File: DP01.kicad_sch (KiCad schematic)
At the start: 18 parts

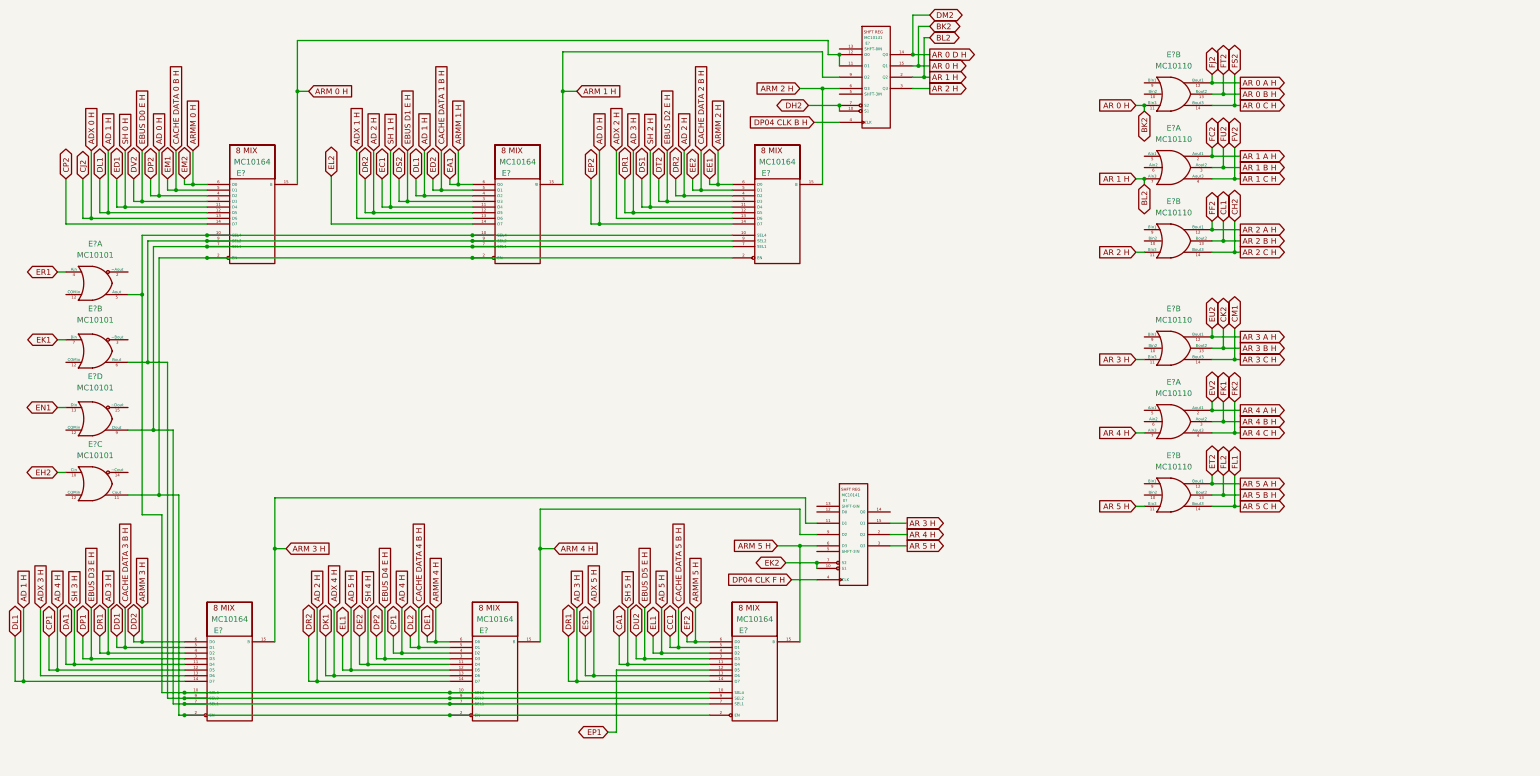
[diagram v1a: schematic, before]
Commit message: EDP is "done" but there is still much work to do to standardize and set up netlist export and verilog creation
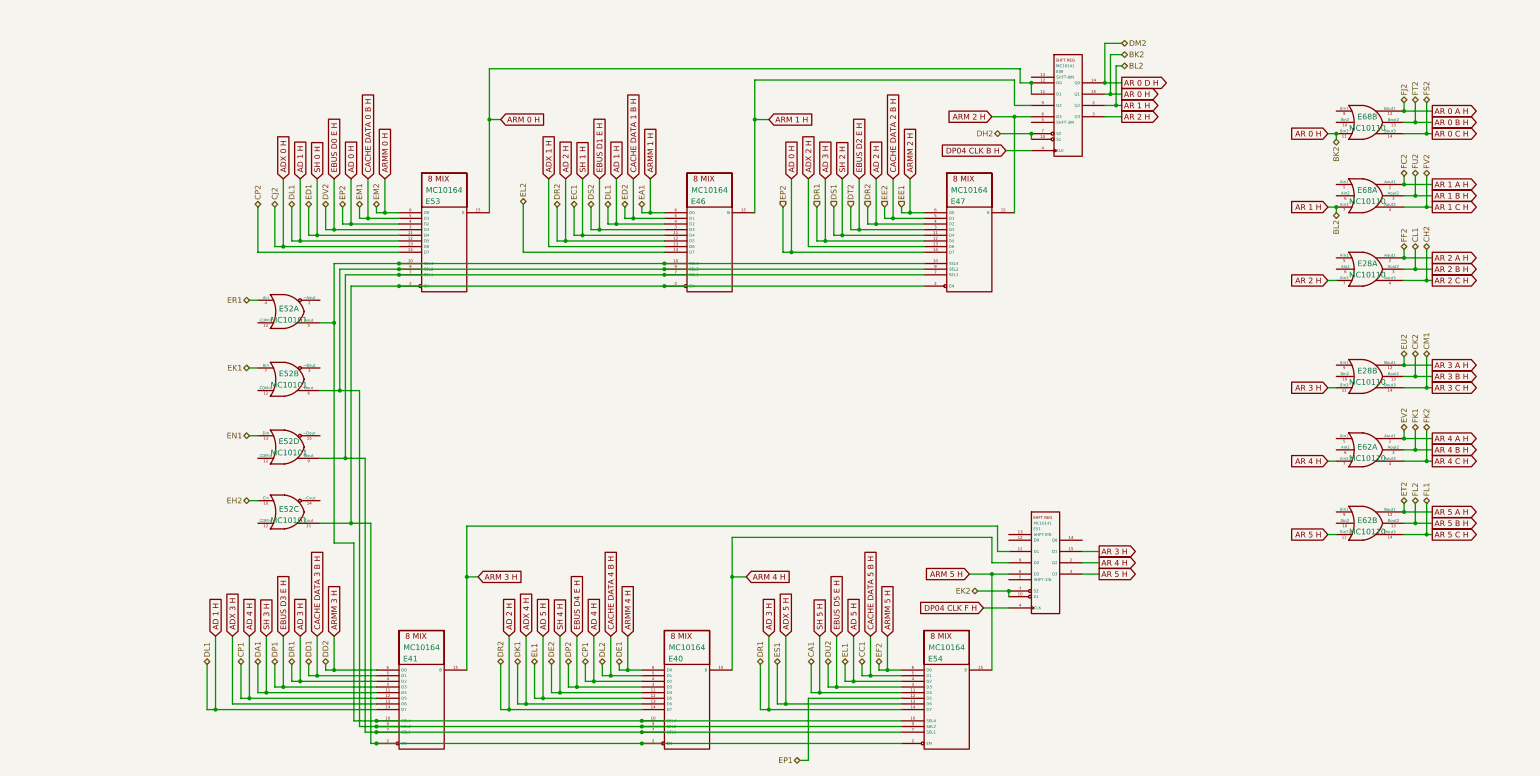
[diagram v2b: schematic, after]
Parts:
- gave numbers to parts that had none: 12
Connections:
- net AD 0 H: no longer E40.3 (D3)
- net AR 2 A H: now also E28.2 (Aout1); no longer E28.12 (Bout1)
- net AR 2 B H: now also E28.3 (Aout2); no longer E28.13 (Bout2)
- net AR 2 C H: now also E28.4 (Aout3); no longer E28.14 (Bout3)
- net AR 2 H: now also E28.7 (Ain3); no longer E28.11 (Bin3)
- net CA1 renamed SH 5 H
- net DA1 renamed SH 3 H
- net DE2 renamed SH 4 H
- net DP1 renamed EBUS D3 E H
- net DS1 renamed SH 2 H
- net DS2 renamed EBUS D1 E H
- net DT2 renamed EBUS D2 E H
- net DU2 renamed EBUS D5 E H
- net DV2 renamed EBUS D0 E H
- net EC1 renamed SH 1 H
- net ED1 renamed SH 0 H
- new net EBUS D4 E H: E40.3 (D3)
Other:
- moved on the sheet: E28A, E28B, E39, E40, E41, E46, E47, E51, E52A, E52B, E52C, E52D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

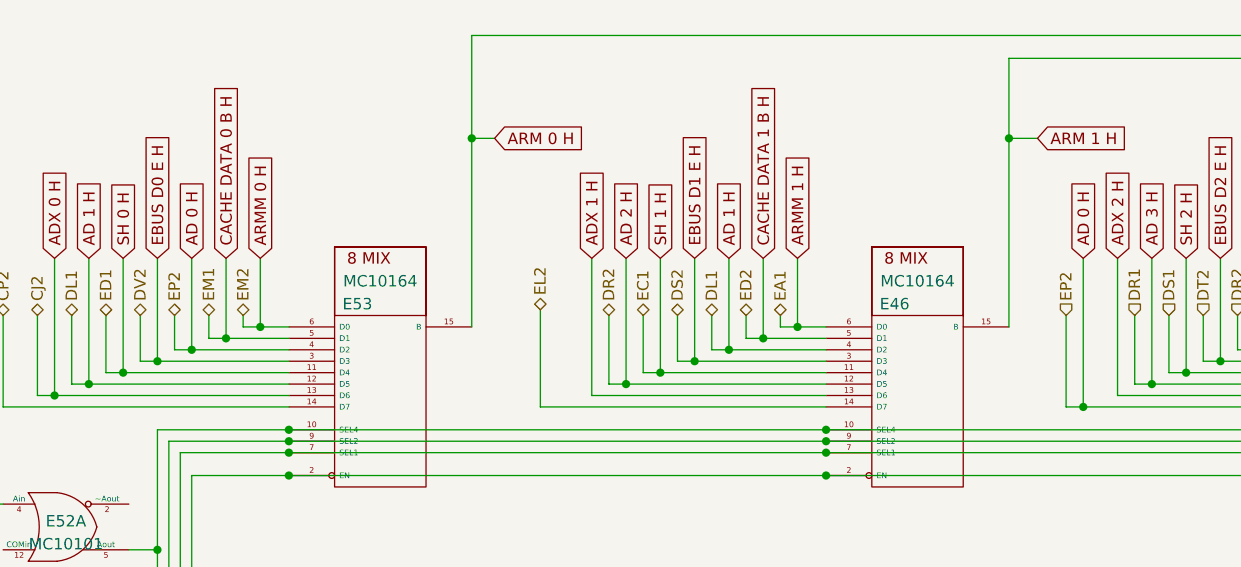
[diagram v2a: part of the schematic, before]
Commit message: Adding backplane connector slowly and painfully
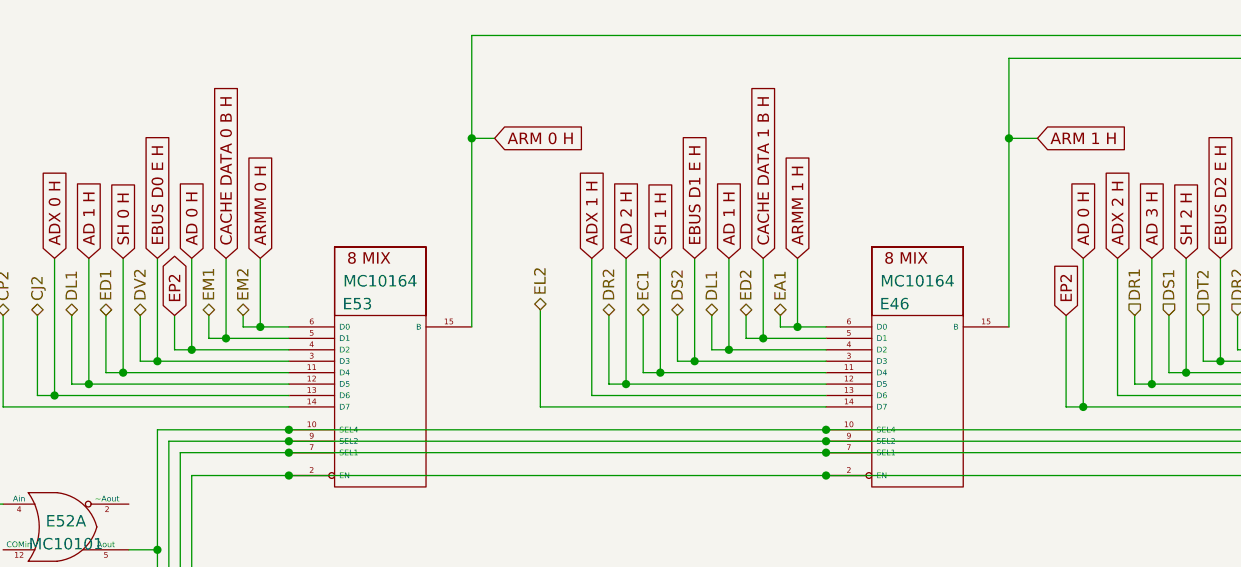
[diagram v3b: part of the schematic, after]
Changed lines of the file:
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@@
+    )
+  )
+  (global_label "EP2" (shape bidirectional) (at 107.315 78.105 90) (fields_autoplaced)
+    (effects (font (size 1.27 1.27)) (justify left))
+    (property "Intersheet References" "${INTERSHEET_REFS}" (id 0) (at 107.2356 72.0633 90)
+      (effects (font (size 1.27 1.27)) (justify left) hide)
     )
   )
@@
     )
   )
+  (global_label "EP2" (shape input) (at 206.375 78.105 90) (fields_autoplaced)
+    (effects (font (size 1.27 1.27)) (justify left))
+    (property "Intersheet References" "${INTERSHEET_REFS}" (id 0) (at 206.2956 72.0633 90)
+      (effects (font (size 1.27 1.27)) (justify left) hide)
+    )
+  )
   (global_label "AR 3 A H" (shape output) (at 352.425 113.665 0) (fields_autoplaced)
     (effects (font (size 1.27 1.27)) (justify left))
@@
     (effects (font (size 1.27 1.27)) (justify left))
   )
-  (hierarchical_label "EP2" (shape bidirectional) (at 107.315 78.105 90)
-    (effects (font (size 1.27 1.27)) (justify left))
-  )
   (hierarchical_label "FC2" (shape bidirectional) (at 346.075 71.12 90)
     (effects (font (size 1.27 1.27)) (justify left))
@@
     (effects (font (size 1.27 1.27)) (justify left))
   )
-  (hierarchical_label "EP2" (shape input) (at 206.375 78.105 90)
-    (effects (font (size 1.27 1.27)) (justify left))
-  )

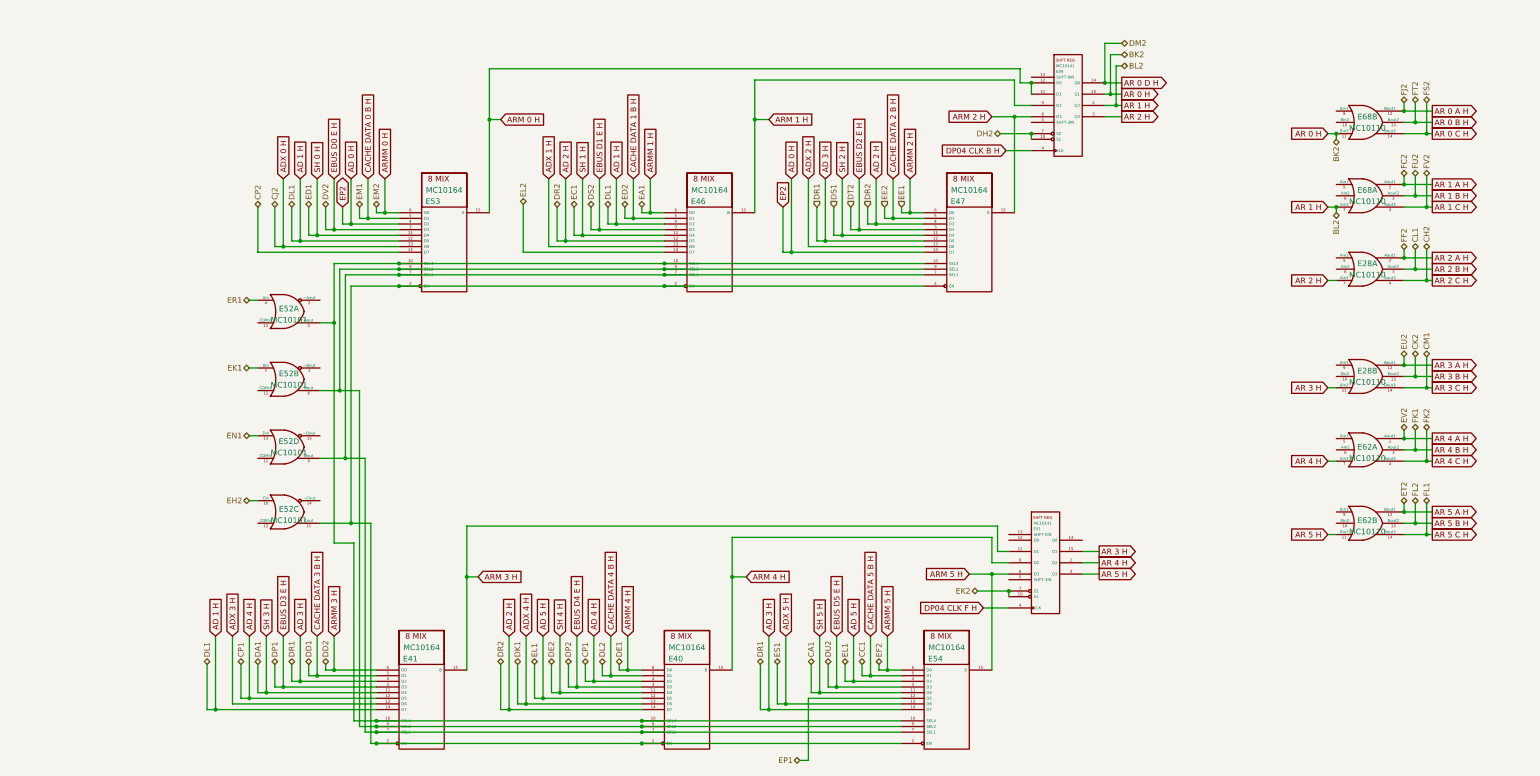
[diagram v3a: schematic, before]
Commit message: Convert all backplane refs to global labels and stick them on J1 pins. Convert all signal labels to global labels too so they are "global" inside M8512 board.
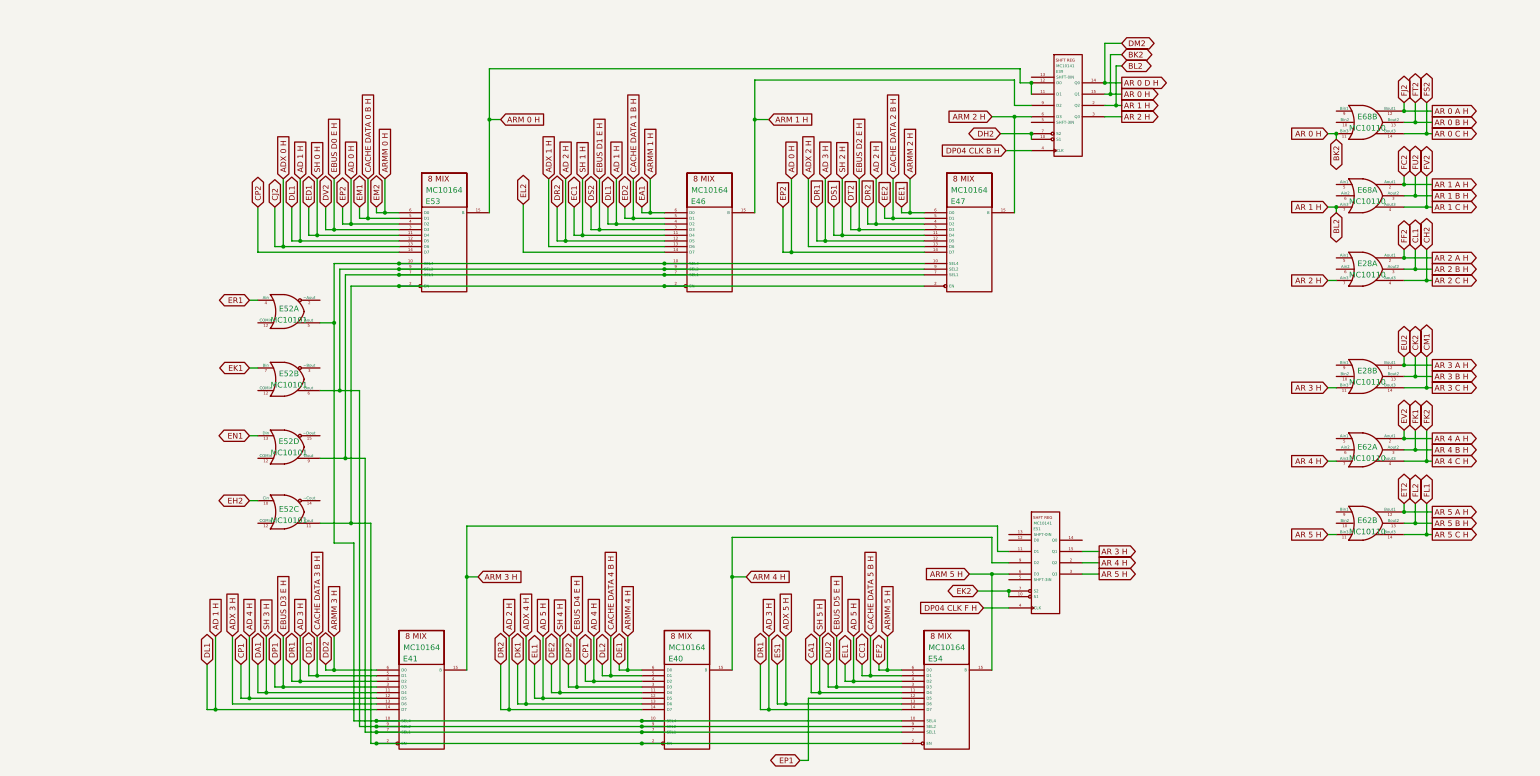
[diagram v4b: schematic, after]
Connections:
- net EBUS D0 E H renamed DV2
- net EBUS D1 E H renamed DS2
- net EBUS D2 E H renamed DT2
- net EBUS D3 E H renamed DP1
- net EBUS D4 E H renamed DP2
- net EBUS D5 E H renamed DU2
- net SH 0 H renamed ED1
- net SH 1 H renamed EC1
- net SH 2 H renamed DS1
- net SH 3 H renamed DA1
- net SH 4 H renamed DE2
- net SH 5 H renamed CA1

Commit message: checkpoint
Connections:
- net AD 0 H renamed AD 0 H <EP2>
- net AD 1 H renamed AD 1 H <DL1>
- net AD 2 H renamed AD 2 H <DR2>
- net AD 3 H renamed AD 3 H <DR1>
- net AD 4 H renamed AD 4 H <CP1>
- net AD 5 H renamed AD 5 H <EL1>
- net ADX 0 H renamed ADX 0 H <CJ2>
- net ADX 4 H renamed ADX 4 H <DK1>
- net ADX 5 H renamed ADX 5 H <ES1>
- net AR 0 A H renamed AR 0 A H <FJ2>
- net AR 0 B H renamed AR 0 B H <FT2>
- net AR 0 C H renamed AR 0 C H <FS2>
- net AR 0 D H renamed AR 0 D H <DM2>
- net AR 0 H renamed AR 0 H <BK2>
- net AR 1 A H renamed AR 1 A H <FC1>
- net AR 1 B H renamed AR 1 B H <FU2>
- net AR 1 C H renamed AR 1 C H <FV2>
- net AR 1 H renamed AR 1 H <BL2>
- net AR 2 A H renamed AR 2 A H <FF2>
- net AR 2 B H renamed AR 2 B H <CL1>
- net AR 2 C H renamed AR 2 C H <CH2>
- net AR 3 A H renamed AR 3 A H <EU2>
- net AR 3 B H renamed AR 3 B H <CK2>
- net AR 3 C H renamed AR 3 C H <CM1>
- net AR 4 A H renamed AR 4 A H <EV2>
- net AR 4 B H renamed AR 4 B H <FK1>
- net AR 4 C H renamed AR 4 C H <FK2>
- net AR 5 A H renamed AR 5 A H <ET2>
- net AR 5 B H renamed AR 5 B H <FL2>
- net AR 5 C H renamed AR 5 C H <FL1>
- net ARMM 0 H renamed ARMM 0 H <EM2>
- net ARMM 1 H renamed ARMM 1 H <EA1>
- net ARMM 2 H renamed ARMM 2 H <EE1>
- net ARMM 3 H renamed ARMM 3 H <DD2>
- net ARMM 4 H renamed ARMM 4 H <DE1>
- net ARMM 5 H renamed ARMM 5 H <EF2>
- net CA1 renamed SH 5 H <CA1>
- net CACHE DATA 0 B H renamed CACHE DATA 0 B H <EM1>
- net CACHE DATA 1 B H renamed CACHE DATA 1 B H <ED2>
- net CACHE DATA 2 B H renamed CACHE DATA 2 B H <EE2>
- net CACHE DATA 3 B H renamed CACHE DATA 3 B H <DD1>
- net CACHE DATA 4 B H renamed CACHE DATA 4 B H <DL2>
- net CACHE DATA 5 B H renamed CACHE DATA 5 B H <CC1>
- net CP2 renamed <CP2>
- net DA1 renamed SH 3 H <DA1>
- net DE2 renamed SH 4 H <DE2>
- net DH2 renamed <DH2>
- net DP1 renamed EBUS D3 E H <DP1>
- net DP2 renamed EBUS D4 E H <DP2>
- net DS1 renamed SH 2 H <DS1>
- net DS2 renamed EBUS D1 E H <DS2>
- net DT2 renamed EBUS D2 E H <DT2>
- net DU2 renamed EBUS D5 E H <DU2>
- net DV2 renamed EBUS D0 E H <DV2>
- net EC1 renamed SH 1 H <EC1>
- net ED1 renamed SH 0 H <ED1>
- net EH2 renamed <EH2>
- net EK1 renamed <EK1>
- net EK2 renamed <EK2>
- net EL2 renamed <EL2>
- net EN1 renamed <EN1>
- net EP1 renamed <EP1>
- net ER1 renamed <ER1>
